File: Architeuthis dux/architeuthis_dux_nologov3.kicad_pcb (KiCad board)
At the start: 2 copper layers, 129.9 x 95.6 mm, 19 parts

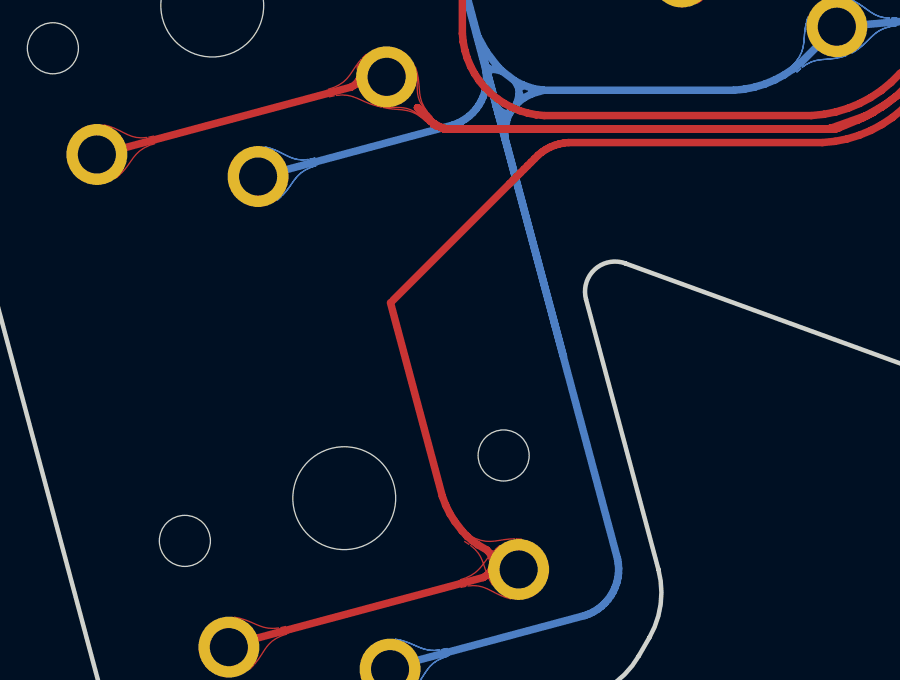
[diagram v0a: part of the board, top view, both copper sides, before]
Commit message: Archive old PCB, update circuits
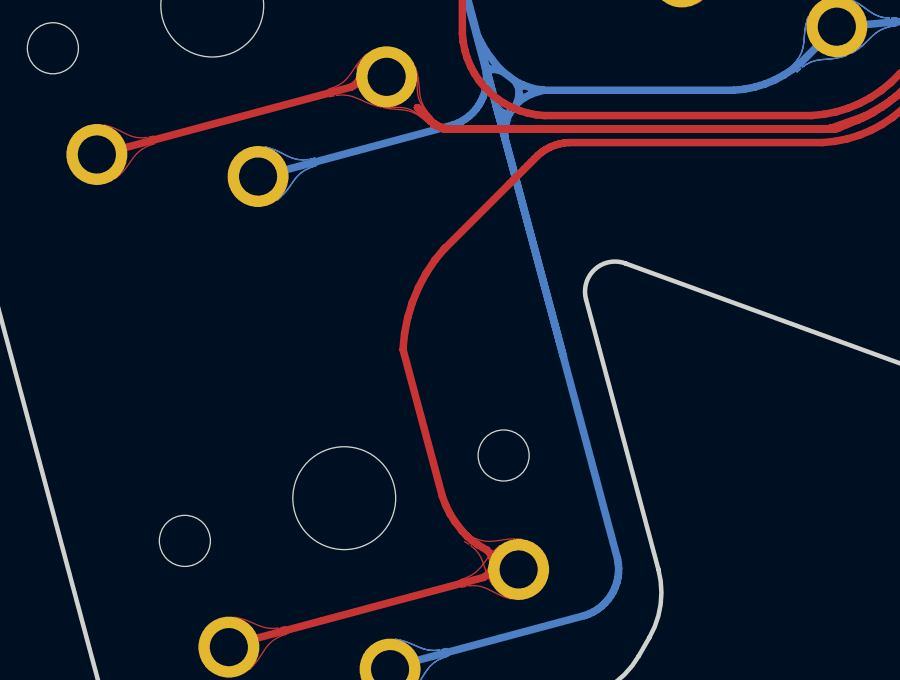
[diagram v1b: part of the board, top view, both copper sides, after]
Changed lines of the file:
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@@
     (thickness 1.6)
     (drawings 58)
-    (tracks 2327)
+    (tracks 2334)
     (zones 0)
     (modules 19)
@@
     (visible_elements 7FFFF7FF)
     (pcbplotparams
-      (layerselection 0x010fc_ffffffff)
+      (layerselection 0x010dc_ffffffff)
       (usegerberextensions true)
       (usegerberattributes false)
@@
       (drillshape 0)
       (scaleselection 1)
-      (outputdirectory "architeuthis_dux_nologogerber"))
+      (outputdirectory "architeuthis_dux_blank"))
   )
   (net 0 "")
@@
   (gr_arc (start 127.509413 110.317406) (end 128.009414 109.45138) (angle -10.00000203) (layer Edge.Cuts) (width 0.15))
   (gr_arc (start 61.427407 86.265522) (end 61.769427 85.325829) (angle -124.999996) (layer Edge.Cuts) (width 0.15))
+  (segment (start 54.67188 86.626726) (end 54.516669 87.138388) (width 0.25) (layer F.Cu) (net 1))
+  (segment (start 54.412358 87.6628) (end 54.35995 88.194911) (width 0.25) (layer F.Cu) (net 1))
+  (segment (start 55.128545 85.661189) (end 54.876496 86.13274) (width 0.25) (layer F.Cu) (net 1))
+  (segment (start 54.516669 87.138388) (end 54.412358 87.6628) (width 0.25) (layer F.Cu) (net 1))
+  (segment (start 55.4256 85.216614) (end 55.128545 85.661189) (width 0.25) (layer F.Cu) (net 1))
+  (segment (start 54.67188 86.626726) (end 54.876496 86.13274) (width 0.25) (layer F.Cu) (net 1))
+  (segment (start 55.764801 84.803297) (end 55.4256 85.216614) (width 0.25) (layer F.Cu) (net 1))
   (segment (start 115.928576 87.98807) (end 116.440238 88.143281) (width 0.25) (layer F.Cu) (net 1))
   (segment (start 144.832498 88.255776) (end 144.383478 88.3) (width 0.25) (layer F.Cu) (net 1))
@@
   (segment (start 57.033315 95.798601) (end 48.543969 98.073315) (width 0.25) (layer F.Cu) (net 1))
   (segment (start 57.154312 94.879532) (end 56.867489 94.713935) (width 0.25) (layer F.Cu) (net 1))
-  (segment (start 55.67368 93.095991) (end 53.942808 86.636286) (width 0.25) (layer F.Cu) (net 1))
   (segment (start 149.687684 78.302086) (end 150.877724 77.112046) (width 0.25) (layer F.Cu) (net 1))
   (segment (start 84.295046 76.991025) (end 89.649928 76.991025) (width 0.25) (layer F.Cu) (net 1))
@@
   (segment (start 59.879675 81.30002) (end 68.341274 81.30002) (width 0.25) (layer F.Cu) (net 1))
   (segment (start 70.998427 80.199393) (end 71.294634 79.903186) (width 0.25) (layer F.Cu) (net 1))
-  (segment (start 57.91209 82.672538) (end 54.02607 86.558558) (width 0.25) (layer F.Cu) (net 1))
+  (segment (start 55.67368 93.095991) (end 54.365648 88.214352) (width 0.25) (layer F.Cu) (net 1))
+  (segment (start 57.91209 82.672538) (end 55.722314 84.862314) (width 0.25) (layer F.Cu) (net 1))
   (segment (start 154.168031 68.101834) (end 154.113021 68.146979) (width 0.25) (layer B.Cu) (net 2))
   (segment (start 124.870449 81.34665) (end 125.283767 81.685851) (width 0.25) (layer B.Cu) (net 2))
